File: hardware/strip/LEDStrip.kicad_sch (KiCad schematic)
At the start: 4 parts, among them J301 WAGO-2065, J302 WAGO-2065, J303 WAGO-2065, U301 74AHC1G125

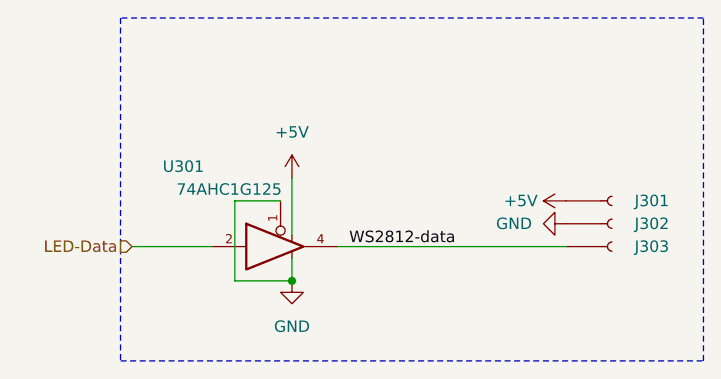
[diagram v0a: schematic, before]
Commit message: Replace Order_Number
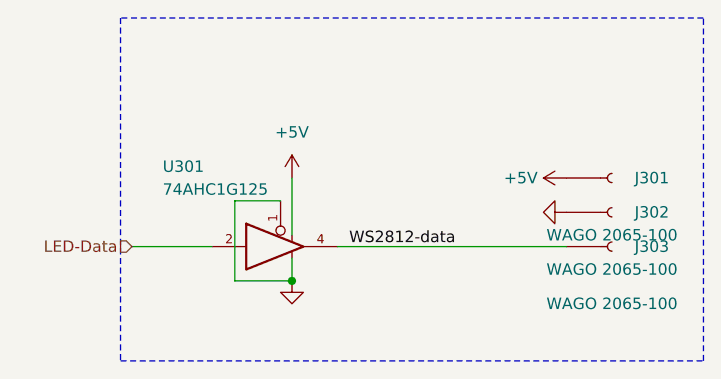
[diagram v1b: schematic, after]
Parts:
- J301, J302, J303: value WAGO-2065 -> WAGO 2065-100; Manufacturer (none) -> WAGO; Product (none) -> 2065-100/998-403
- U301: footprint Package_TO_SOT_SMD:SOT-23-5 -> V2_Package_TO_SOT_SMD:SOT-23-5; Manufacturer (none) -> Texas Instruments; Mouser (none) -> 595-SN74AHC1G125DBVR; Product (none) -> SN74AHC1G125DBVR
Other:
- moved on the sheet: J301, J302
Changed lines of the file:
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@@
 (kicad_sch
-	(version 20231120)
+	(version 20250114)
 	(generator "eeschema")
-	(generator_version "8.0")
+	(generator_version "9.0")
 	(paper "A4")
 	(title_block
 		(title "LED Strip")
-		(date "2023-01-12")
+		(date "2026-02-11")
+		(rev "2026-02-11")
 		(company "Versio Duo")
 	)
@@
 	(label "WS2812-data"
 		(at 146.05 111.76 0)
-		(fields_autoplaced yes)
 		(effects
 			(font
@@
 		(shape input)
 		(at 121.92 111.76 180)
-		(fields_autoplaced yes)
 		(effects
 			(font
@@
 	)
 	(symbol
-		(lib_id "power:GND")
-		(at 170.18 109.22 270)
+		(lib_id "V2_power:GND")
+		(at 170.18 107.95 270)
 		(unit 1)
 		(exclude_from_sim no)
@@
 		(on_board yes)
 		(dnp no)
-		(fields_autoplaced yes)
 		(property "Reference" "#PWR0304"
-			(at 163.83 109.22 0)
+			(at 163.83 107.95 0)
 			(effects
 				(font
@@
 		)
 		(property "Value" "GND"
-			(at 166.37 109.2199 90)
+			(at 166.37 107.9499 90)
 			(effects
 				(font
@@
 				)
 				(justify right)
+				(hide yes)
 			)
 		)
 		(property "Footprint" ""
-			(at 170.18 109.22 0)
+			(at 170.18 107.95 0)
 			(effects
 				(font
@@
 		)
 		(property "Datasheet" ""
-			(at 170.18 109.22 0)
+			(at 170.18 107.95 0)
 			(effects
 				(font
@@
 		)
 		(property "Description" ""
-			(at 170.18 109.22 0)
+			(at 170.18 107.95 0)
 			(effects
 				(font
@@
 	(symbol
 		(lib_id "V2_Connector_WAGO:2065")
-		(at 175.26 109.22 0)
+		(at 175.26 107.95 0)
 		(unit 1)
-		(exclude_from_sim yes)
+		(exclude_from_sim no)
 		(in_bom yes)
 		(on_board yes)
 		(dnp no)
 		(property "Reference" "J302"
-			(at 181.61 109.22 0)
+			(at 181.61 107.95 0)
 			(effects
 				(font
@@
 			)
 		)
-		(property "Value" "WAGO-2065"
-			(at 175.26 115.57 0)
-			(effects
-				(font
-					(size 1.27 1.27)
-				)
-				(hide yes)
+		(property "Value" "WAGO 2065-100"
+			(at 175.26 114.3 0)
+			(effects
+				(font
+					(size 1.27 1.27)
+				)
 			)
 		)
 		(property "Footprint" "V2_Connector_WAGO:2065-100"
-			(at 175.26 113.03 0)
+			(at 175.26 111.76 0)
 			(effects
 				(font
@@
 		)
 		(property "Datasheet" ""
-			(at 175.26 113.03 0)
+			(at 175.26 111.76 0)
 			(effects
 				(font
@@
 		)
 		(property "Description" ""
-			(at 175.26 109.22 0)
+			(at 175.26 107.95 0)
+			(effects
+				(font
+					(size 1.27 1.27)
+				)
+				(hide yes)
+			)
+		)
+		(property "Manufacturer" "WAGO"
+			(at 175.26 121.158 0)
+			(effects
+				(font
+					(size 1.27 1.27)
+				)
+				(hide yes)
+			)
+		)
+		(property "Product" "2065-100/998-403"
+			(at 175.26 124.46 0)
 			(effects
 				(font
@@
 	)
 	(symbol
-		(lib_id "power:+5V")
+		(lib_id "V2_power:+5V")
 		(at 139.7 104.14 0)
 		(unit 1)
@@
 	)
 	(symbol
-		(lib_id "power:+5V")
-		(at 170.18 106.68 90)
+		(lib_id "V2_power:+5V")
+		(at 170.18 104.14 90)
 		(unit 1)
 		(exclude_from_sim no)
@@
 		(fields_autoplaced yes)
 		(property "Reference" "#PWR0303"
-			(at 173.99 106.68 0)
+			(at 173.99 104.14 0)
 			(effects
 				(font
@@
 		)
 		(property "Value" "+5V"
-			(at 167.005 106.6799 90)
+			(at 167.005 104.1399 90)
 			(effects
 				(font
@@
 		)
 		(property "Footprint" ""
-			(at 170.18 106.68 0)
+			(at 170.18 104.14 0)
 			(effects
 				(font
@@
 		)
 		(property "Datasheet" ""
-			(at 170.18 106.68 0)
+			(at 170.18 104.14 0)
 			(effects
 				(font
@@
 		)
 		(property "Description" ""
-			(at 170.18 106.68 0)
+			(at 170.18 104.14 0)
 			(effects
 				(font
@@
 	)
 	(symbol
-		(lib_id "power:GND")
+		(lib_id "V2_power:GND")
 		(at 139.7 115.57 0)
 		(unit 1)
@@
 					(size 1.27 1.27)
 				)
+				(hide yes)
 			)
 		)
@@
 		(at 175.26 111.76 0)
 		(unit 1)
-		(exclude_from_sim yes)
+		(exclude_from_sim no)
 		(in_bom yes)
 		(on_board yes)
@@
 			)
 		)
-		(property "Value" "WAGO-2065"
+		(property "Value" "WAGO 2065-100"
 			(at 175.26 118.11 0)
 			(effects
@@
 					(size 1.27 1.27)
 				)
-				(hide yes)
 			)
 		)
@@
 		(property "Description" ""
 			(at 175.26 111.76 0)
+			(effects
+				(font
+					(size 1.27 1.27)
+				)
+				(hide yes)
+			)
+		)
+		(property "Manufacturer" "WAGO"
+			(at 175.26 124.968 0)
+			(effects
+				(font
+					(size 1.27 1.27)
+				)
+				(hide yes)
+			)
+		)
+		(property "Product" "2065-100/998-403"
+			(at 175.26 128.27 0)
 			(effects
 				(font
@@
 		)
 		(property "Value" "74AHC1G125"
-			(at 132.715 105.41 0)
-			(effects
-				(font
-					(size 1.27 1.27)
-				)
-			)
-		)
-		(property "Footprint" "Package_TO_SOT_SMD:SOT-23-5"
+			(at 131.191 105.41 0)
+			(effects
+				(font
+					(size 1.27 1.27)
+				)
+			)
+		)
+		(property "Footprint" "V2_Package_TO_SOT_SMD:SOT-23-5"
 			(at 138.43 111.76 0)
 			(effects
@@
 			)
 		)
-		(property "Description" ""
+		(property "Description" "Single Buffer Gate Tri-State, Low-Voltage CMOS"
 			(at 138.43 111.76 0)
+			(effects
+				(font
+					(size 1.27 1.27)
+				)
+				(hide yes)
+			)
+		)
+		(property "Mouser" "595-SN74AHC1G125DBVR"
+			(at 138.43 139.7 0)
+			(effects
+				(font
+					(size 1.27 1.27)
+				)
+				(hide yes)
+			)
+		)
+		(property "Product" "SN74AHC1G125DBVR"
+			(at 138.43 137.16 0)
+			(effects
+				(font
+					(size 1.27 1.27)
+				)
+				(hide yes)
+			)
+		)
+		(property "Manufacturer" "Texas Instruments"
+			(at 138.43 134.62 0)
 			(effects
 				(font
@@
 	(symbol
 		(lib_id "V2_Connector_WAGO:2065")
-		(at 175.26 106.68 0)
+		(at 175.26 104.14 0)
 		(unit 1)
-		(exclude_from_sim yes)
+		(exclude_from_sim no)
 		(in_bom yes)
 		(on_board yes)
 		(dnp no)
 		(property "Reference" "J301"
-			(at 181.6101 106.68 0)
+			(at 181.6101 104.14 0)
 			(effects
 				(font
@@
 			)
 		)
-		(property "Value" "WAGO-2065"
-			(at 175.26 113.03 0)
-			(effects
-				(font
-					(size 1.27 1.27)
-				)
-				(hide yes)
+		(property "Value" "WAGO 2065-100"
+			(at 175.26 110.49 0)
+			(effects
+				(font
+					(size 1.27 1.27)
+				)
 			)
 		)
 		(property "Footprint" "V2_Connector_WAGO:2065-100"
-			(at 175.26 110.49 0)
+			(at 175.26 107.95 0)
 			(effects
 				(font
@@
 		)
 		(property "Datasheet" ""
-			(at 175.26 110.49 0)
+			(at 175.26 107.95 0)
 			(effects
 				(font
@@
 		)
 		(property "Description" ""
-			(at 175.26 106.68 0)
-			(effects
-				(font
+			(at 175.26 104.14 0)
+			(effects
+				(font
+					(size 1.27 1.27)
+				)
+				(hide yes)
+			)
+		)
+		(property "Manufacturer" "WAGO"
+			(at 175.26 117.348 0)
+			(effects
+				(font
+					(size 1.27 1.27)
+				)
+				(hide yes)
+			)
+		)
+		(property "Product" "2065-100/998-403"
+			(at 175.26 120.65 0)
+			(effects
+				(font

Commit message: Update
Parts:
- J201: renamed from J301; Id (none) -> WAGO:${SYMBOL_NAME}; Rating (none) -> 9A
- J202: renamed from J302; Id (none) -> WAGO:${SYMBOL_NAME}; Rating (none) -> 9A
- J203: renamed from J303; Id (none) -> WAGO:${SYMBOL_NAME}; Rating (none) -> 9A
- U201: renamed from U301; Id (none) -> 74xGxx:${SYMBOL_NAME}; Rating (none) -> 8mA
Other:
- title: LED Strip -> V2 strip
